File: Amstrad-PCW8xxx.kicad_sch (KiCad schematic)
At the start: 103 parts, among them IC101 GateArray, IC102 Z80A, IC103 74HCU04, IC120 TC74HC14, IC201 SED9420AC, IC202 74HC00, IC204 74HC04, IC205 74HC04, J101 Printer Power, X101 32MHz, X201 18MHz, X701 11MHz

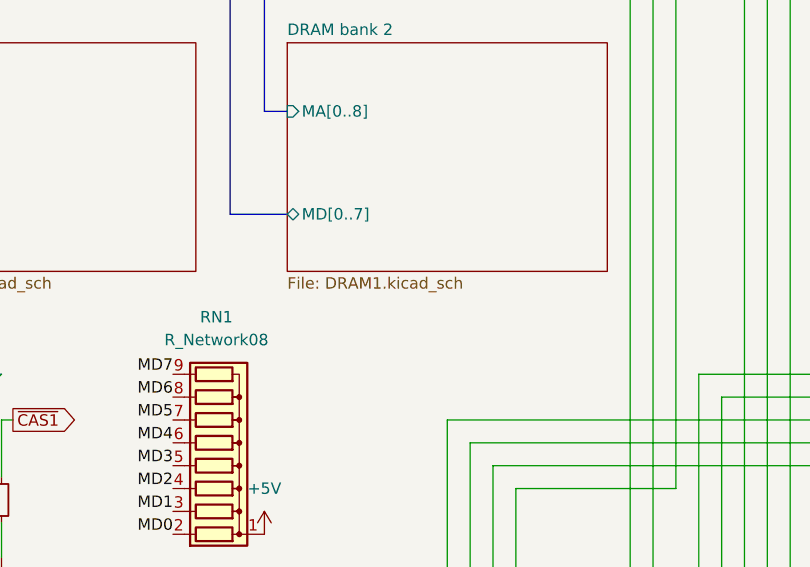
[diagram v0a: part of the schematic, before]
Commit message: fix shared schematic across dram pages
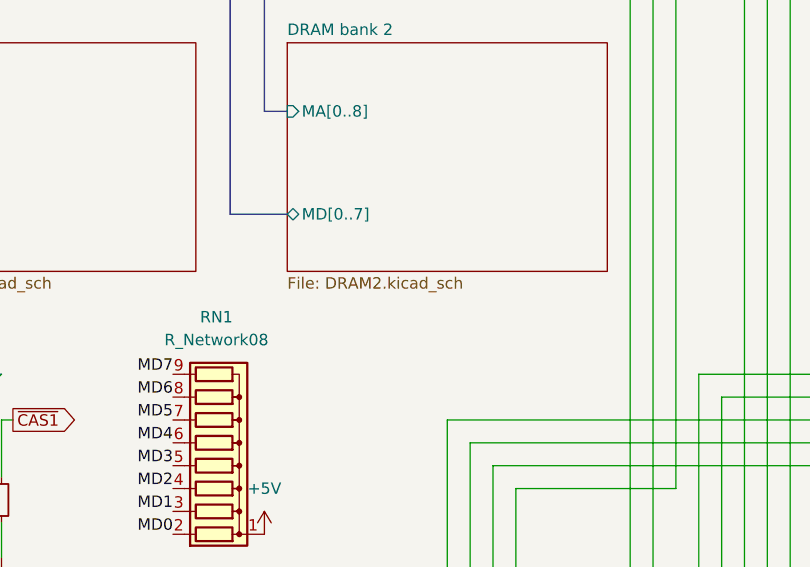
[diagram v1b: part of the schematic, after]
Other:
- sheet DRAM bank 2: file DRAM1.kicad_sch -> DRAM2.kicad_sch
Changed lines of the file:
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@@
 			)
 		)
-		(property "Sheetfile" "DRAM1.kicad_sch"
+		(property "Sheetfile" "DRAM2.kicad_sch"
 			(at 242.57 146.6346 0)
 			(show_name no)

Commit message: fix incorrect gate array pin numbering
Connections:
- net +5V: now also IC102.11 (V_{CC})
- net MA5: now also R115.1
- net ~{CAS1}: no longer R104.1
- net at R103.2: now also IC101.8 (~{MWE}); no longer IC101.19 (~{MWE})
- net at R105.2: now also IC101.16 (~{CAS1}); no longer IC101.8 (~{CAS1})
- net at IC203.16 (TC): now also IC101.18 (TC); no longer IC101.16 (TC)
- net at IC203.2 (~{RD}): now also IC101.19 (~{DIORD}); no longer IC101.18 (~{DIORD})
- net at R115.2: now also IC101.36 (MA5)
- new net ~{CAS2}: R104.1
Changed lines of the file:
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@@
 	)
 	(no_connect
-		(at 90.17 177.8)
+		(at 90.17 172.72)
 	)
 	(no_connect
@@
 	)
 	(no_connect
-		(at 92.71 177.8)
+		(at 92.71 172.72)
 	)
 	(no_connect
@@
 	(wire
 		(pts
+			(xy 158.75 172.72) (xy 158.75 177.8)
+		)
+		(stroke
+			(width 0)
+			(type default)
+		)
+	)
+	(wire
+		(pts
 			(xy 49.53 180.34) (xy 74.93 180.34)
 		)
@@
 	(wire
 		(pts
-			(xy 158.75 160.02) (xy 158.75 163.83)
+			(xy 158.75 160.02) (xy 158.75 167.64)
 		)
 		(stroke
@@
 		)
 	)
-	(global_label "~{CAS1}"
+	(global_label "~{CAS2}"
 		(shape output)
 		(at 212.09 162.56 0)
@@
 	(symbol
 		(lib_id "power:+5V")
-		(at 87.63 177.8 0)
+		(at 87.63 172.72 0)
 		(unit 1)
 		(body_style 1)
@@
 		(fields_autoplaced yes)
 		(property "Reference" "#PWR010"
-			(at 87.63 181.61 0)
+			(at 87.63 176.53 0)
 			(hide yes)
 			(show_name no)
@@
 		)
 		(property "Value" "+5V"
-			(at 87.63 172.72 0)
+			(at 87.63 167.64 0)
 			(show_name no)
 			(do_not_autoplace no)
@@
 		)
 		(property "Footprint" ""
-			(at 87.63 177.8 0)
+			(at 87.63 172.72 0)
 			(hide yes)
 			(show_name no)
@@
 		)
 		(property "Datasheet" ""
-			(at 87.63 177.8 0)
+			(at 87.63 172.72 0)
 			(hide yes)
 			(show_name no)
@@
 		)
 		(property "Description" "Power symbol creates a global label with name \"+5V\""
-			(at 87.63 177.8 0)
+			(at 87.63 172.72 0)
 			(hide yes)
 			(show_name no)
@@
 	(symbol
 		(lib_id "Device:R_Small")
-		(at 158.6374 170.135 0)
+		(at 158.75 170.18 0)
 		(unit 1)
 		(body_style 1)
@@
 		(dnp no)
 		(property "Reference" "R115"
-			(at 157.6214 176.4849 90)
+			(at 157.734 176.5299 90)
 			(show_name no)
 			(do_not_autoplace no)
@@
 		)
 		(property "Value" "33R"
-			(at 157.6214 167.8489 90)
+			(at 157.734 167.8939 90)
 			(show_name no)
 			(do_not_autoplace no)
@@
 		)
 		(property "Footprint" ""
-			(at 158.6374 170.135 0)
+			(at 158.75 170.18 0)
 			(hide yes)
 			(show_name no)
@@
 		)
 		(property "Datasheet" ""
-			(at 158.6374 170.135 0)
+			(at 158.75 170.18 0)
 			(hide yes)
 			(show_name no)
@@
 		)
 		(property "Description" "Resistor, small symbol"
-			(at 158.6374 170.135 0)
+			(at 158.75 170.18 0)
 			(hide yes)
 			(show_name no)

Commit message: outline pcb
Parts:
- removed C201: 100nF, symbol Device:C_Small
- removed CP103: Keyboard Connector, symbol Connector:DIN-4
- added CP103: Keyboard Connection, Connector_Molex:Molex_KK-254_AE-6410-04A_1x04_P2.54mm_Vertical, symbol Connector_Generic:Conn_01x04
- C101, C102, C103, C104, C105, C106, C107, C108, C109, C110, C111, C112, C113, C114, C115, C116, C117, C118, C119, C120, C126, C127, C128, C201, C202, C203, C204, C205, C206, C207, C208, C209, C210, C701, C702, C703: footprint (none) -> Capacitor_THT:C_Disc_D10.0mm_W2.5mm_P5.00mm
- C121: footprint (none) -> Capacitor_THT:CP_Radial_D10.0mm_P5.00mm; now left out of the parts list
- C122, C123, C124: footprint (none) -> Capacitor_THT:CP_Radial_D10.0mm_P5.00mm
- CD201, CD202, CP101: footprint (none) -> Connector_Molex:Molex_KK-254_AE-6410-04A_1x04_P2.54mm_Vertical
- CD203: footprint (none) -> Connector_IDC:IDC-Header_2x13_P2.54mm_Horizontal
- CP706: footprint Connector_PinSocket_2.54mm:PinSocket_2x17_P2.54mm_Horizontal -> Connector_IDC:IDC-Header_2x17_P2.54mm_Horizontal
- IC101: footprint (none) -> Package_QFP:Hitachi_FP80B_PQFP-80_14x20mm_P0.8mm
- IC103, IC120, IC202, IC204, IC205: footprint (none) -> Package_DIP:DIP-14_W7.62mm
- IC201: footprint (none) -> Package_DIP:DIP-24_18.0mmx34.29mm_W15.24mm
- IC203: value (none) -> D765AC-2; footprint (none) -> Package_DIP:DIP-40_W15.24mm
- IC701: value (none) -> 40026; footprint (none) -> Package_DIP:DIP-40_W15.24mm
- NR103: renamed from RN1; value R_Network08 -> 10K
- R101, R102, R103, R104, R105, R106, R107, R108, R109, R110, R111, R112, R113, R114, R115, R116, R117, R118, R119, R120, R122, R123, R124, R201, R202, R203, R204, R206, R701, R725: footprint (none) -> Resistor_THT:R_Axial_DIN0207_L6.3mm_D2.5mm_P10.16mm_Horizontal
- X101: footprint (none) -> Crystal:Crystal_HC49-U_Horizontal_1EP_style2
- X201, X701: footprint (none) -> Crystal:Crystal_HC52-8mm_Vertical
- renumbered NR202 to NR102
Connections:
- net +5V: now also CP103.2 (Pin_2)
- net GND: now also CP103.1 (Pin_1)
- net K3: now also CP103.3 (Pin_3)
- net K4: now also CP103.4 (Pin_4)
- net at IC202.10, IC203.39 (~{RW}/SEEK), NR201.8 (R7): now also IC202.12
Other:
- moved on the sheet: IC204B, IC204E, IC205A, IC205B

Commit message: progress PCB layout
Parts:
- C101, C102, C103, C104, C105, C106, C107, C108, C109, C110, C111, C112, C113, C114, C115, C116, C117, C118, C119, C120, C126, C127, C128, C201, C202, C203, C204, C205, C206, C207, C208, C209, C210, C701, C702, C703: footprint Capacitor_THT:C_Disc_D10.0mm_W2.5mm_P5.00mm -> Library:C_Disc_D9.0mm_W2.5mm_P5.00mm
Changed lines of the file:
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@@
 			)
 		)
-		(property "Footprint" "Capacitor_THT:C_Disc_D10.0mm_W2.5mm_P5.00mm"
+		(property "Footprint" "Library:C_Disc_D9.0mm_W2.5mm_P5.00mm"
 			(at 170.18 323.85 0)
 			(hide yes)
@@
 			)
 		)
-		(property "Footprint" "Capacitor_THT:C_Disc_D10.0mm_W2.5mm_P5.00mm"
+		(property "Footprint" "Library:C_Disc_D9.0mm_W2.5mm_P5.00mm"
 			(at 223.52 323.85 0)
 			(hide yes)
@@
 			)
 		)
-		(property "Footprint" "Capacitor_THT:C_Disc_D10.0mm_W2.5mm_P5.00mm"
+		(property "Footprint" "Library:C_Disc_D9.0mm_W2.5mm_P5.00mm"
 			(at 193.04 323.85 0)
 			(hide yes)
@@
 			)
 		)
-		(property "Footprint" "Capacitor_THT:C_Disc_D10.0mm_W2.5mm_P5.00mm"
+		(property "Footprint" "Library:C_Disc_D9.0mm_W2.5mm_P5.00mm"
 			(at 215.9 323.85 0)
 			(hide yes)
@@
 			)
 		)
-		(property "Footprint" "Capacitor_THT:C_Disc_D10.0mm_W2.5mm_P5.00mm"
+		(property "Footprint" "Library:C_Disc_D9.0mm_W2.5mm_P5.00mm"
 			(at 447.04 294.64 0)
 			(hide yes)
@@
 			)
 		)
-		(property "Footprint" "Capacitor_THT:C_Disc_D10.0mm_W2.5mm_P5.00mm"
+		(property "Footprint" "Library:C_Disc_D9.0mm_W2.5mm_P5.00mm"
 			(at 471.17 226.06 0)
 			(hide yes)
@@
 			)
 		)
-		(property "Footprint" "Capacitor_THT:C_Disc_D10.0mm_W2.5mm_P5.00mm"
+		(property "Footprint" "Library:C_Disc_D9.0mm_W2.5mm_P5.00mm"
 			(at 88.9 120.65 0)
 			(hide yes)
@@
 			)
 		)
-		(property "Footprint" "Capacitor_THT:C_Disc_D10.0mm_W2.5mm_P5.00mm"
+		(property "Footprint" "Library:C_Disc_D9.0mm_W2.5mm_P5.00mm"
 			(at 162.56 334.01 0)
 			(hide yes)
@@
 			)
 		)
-		(property "Footprint" "Capacitor_THT:C_Disc_D10.0mm_W2.5mm_P5.00mm"
+		(property "Footprint" "Library:C_Disc_D9.0mm_W2.5mm_P5.00mm"
 			(at 473.71 250.19 0)
 			(hide yes)
@@
 			)
 		)
-		(property "Footprint" "Capacitor_THT:C_Disc_D10.0mm_W2.5mm_P5.00mm"
+		(property "Footprint" "Library:C_Disc_D9.0mm_W2.5mm_P5.00mm"
 			(at 200.66 323.85 0)
 			(hide yes)
@@
 			)
 		)
-		(property "Footprint" "Capacitor_THT:C_Disc_D10.0mm_W2.5mm_P5.00mm"
+		(property "Footprint" "Library:C_Disc_D9.0mm_W2.5mm_P5.00mm"
 			(at 208.28 323.85 0)
 			(hide yes)
@@
 			)
 		)
-		(property "Footprint" "Capacitor_THT:C_Disc_D10.0mm_W2.5mm_P5.00mm"
+		(property "Footprint" "Library:C_Disc_D9.0mm_W2.5mm_P5.00mm"
 			(at 238.76 323.85 0)
 			(hide yes)
@@
 			)
 		)
-		(property "Footprint" "Capacitor_THT:C_Disc_D10.0mm_W2.5mm_P5.00mm"
+		(property "Footprint" "Library:C_Disc_D9.0mm_W2.5mm_P5.00mm"
 			(at 299.72 294.64 0)
 			(hide yes)
@@
 			)
 		)
-		(property "Footprint" "Capacitor_THT:C_Disc_D10.0mm_W2.5mm_P5.00mm"
+		(property "Footprint" "Library:C_Disc_D9.0mm_W2.5mm_P5.00mm"
 			(at 254 323.85 0)
 			(hide yes)
@@
 			)
 		)
-		(property "Footprint" "Capacitor_THT:C_Disc_D10.0mm_W2.5mm_P5.00mm"
+		(property "Footprint" "Library:C_Disc_D9.0mm_W2.5mm_P5.00mm"
 			(at 469.9 260.35 0)
 			(hide yes)
@@
 			)
 		)
-		(property "Footprint" "Capacitor_THT:C_Disc_D10.0mm_W2.5mm_P5.00mm"
+		(property "Footprint" "Library:C_Disc_D9.0mm_W2.5mm_P5.00mm"
 			(at 276.86 323.85 0)
 			(hide yes)
@@
 			)
 		)
-		(property "Footprint" "Capacitor_THT:C_Disc_D10.0mm_W2.5mm_P5.00mm"
+		(property "Footprint" "Library:C_Disc_D9.0mm_W2.5mm_P5.00mm"
 			(at 185.42 323.85 0)
 			(hide yes)
@@
 			)
 		)
-		(property "Footprint" "Capacitor_THT:C_Disc_D10.0mm_W2.5mm_P5.00mm"
+		(property "Footprint" "Library:C_Disc_D9.0mm_W2.5mm_P5.00mm"
 			(at 246.38 323.85 0)
 			(hide yes)
@@
 			)
 		)
-		(property "Footprint" "Capacitor_THT:C_Disc_D10.0mm_W2.5mm_P5.00mm"
+		(property "Footprint" "Library:C_Disc_D9.0mm_W2.5mm_P5.00mm"
 			(at 68.58 130.81 0)
 			(hide yes)
@@
 			)
 		)
-		(property "Footprint" "Capacitor_THT:C_Disc_D10.0mm_W2.5mm_P5.00mm"
+		(property "Footprint" "Library:C_Disc_D9.0mm_W2.5mm_P5.00mm"
 			(at 231.14 323.85 0)
 			(hide yes)
@@
 			)
 		)
-		(property "Footprint" "Capacitor_THT:C_Disc_D10.0mm_W2.5mm_P5.00mm"
+		(property "Footprint" "Library:C_Disc_D9.0mm_W2.5mm_P5.00mm"
 			(at 147.32 323.85 0)
 			(hide yes)
@@
 			)
 		)
-		(property "Footprint" "Capacitor_THT:C_Disc_D10.0mm_W2.5mm_P5.00mm"
+		(property "Footprint" "Library:C_Disc_D9.0mm_W2.5mm_P5.00mm"
 			(at 177.8 323.85 0)
 			(hide yes)
@@
 			)
 		)
-		(property "Footprint" "Capacitor_THT:C_Disc_D10.0mm_W2.5mm_P5.00mm"
+		(property "Footprint" "Library:C_Disc_D9.0mm_W2.5mm_P5.00mm"
 			(at 471.17 238.76 0)
 			(hide yes)
@@
 			)
 		)
-		(property "Footprint" "Capacitor_THT:C_Disc_D10.0mm_W2.5mm_P5.00mm"
+		(property "Footprint" "Library:C_Disc_D9.0mm_W2.5mm_P5.00mm"
 			(at 139.7 323.85 0)
 			(hide yes)
@@
 			)
 		)
-		(property "Footprint" "Capacitor_THT:C_Disc_D10.0mm_W2.5mm_P5.00mm"
+		(property "Footprint" "Library:C_Disc_D9.0mm_W2.5mm_P5.00mm"
 			(at 269.24 323.85 0)
 			(hide yes)
@@
 			)
 		)
-		(property "Footprint" "Capacitor_THT:C_Disc_D10.0mm_W2.5mm_P5.00mm"
+		(property "Footprint" "Library:C_Disc_D9.0mm_W2.5mm_P5.00mm"
 			(at 162.56 323.85 0)
 			(hide yes)
@@
 			)
 		)
-		(property "Footprint" "Capacitor_THT:C_Disc_D10.0mm_W2.5mm_P5.00mm"
+		(property "Footprint" "Library:C_Disc_D9.0mm_W2.5mm_P5.00mm"
 			(at 132.08 323.85 0)
 			(hide yes)
@@
 			)
 		)
-		(property "Footprint" "Capacitor_THT:C_Disc_D10.0mm_W2.5mm_P5.00mm"
+		(property "Footprint" "Library:C_Disc_D9.0mm_W2.5mm_P5.00mm"
 			(at 147.32 334.01 0)
 			(hide yes)
@@
 			)
 		)
-		(property "Footprint" "Capacitor_THT:C_Disc_D10.0mm_W2.5mm_P5.00mm"
+		(property "Footprint" "Library:C_Disc_D9.0mm_W2.5mm_P5.00mm"
 			(at 154.94 334.01 0)
 			(hide yes)
@@
 			)
 		)
-		(property "Footprint" "Capacitor_THT:C_Disc_D10.0mm_W2.5mm_P5.00mm"
+		(property "Footprint" "Library:C_Disc_D9.0mm_W2.5mm_P5.00mm"
 			(at 487.68 254 0)
 			(hide yes)
@@
 			)
 		)
-		(property "Footprint" "Capacitor_THT:C_Disc_D10.0mm_W2.5mm_P5.00mm"
+		(property "Footprint" "Library:C_Disc_D9.0mm_W2.5mm_P5.00mm"
 			(at 307.34 298.45 0)
 			(hide yes)
@@
 			)
 		)
-		(property "Footprint" "Capacitor_THT:C_Disc_D10.0mm_W2.5mm_P5.00mm"
+		(property "Footprint" "Library:C_Disc_D9.0mm_W2.5mm_P5.00mm"
 			(at 154.94 323.85 0)
 			(hide yes)
@@
 			)
 		)
-		(property "Footprint" "Capacitor_THT:C_Disc_D10.0mm_W2.5mm_P5.00mm"
+		(property "Footprint" "Library:C_Disc_D9.0mm_W2.5mm_P5.00mm"
 			(at 261.62 323.85 0)
 			(hide yes)
@@
 			)
 		)
-		(property "Footprint" "Capacitor_THT:C_Disc_D10.0mm_W2.5mm_P5.00mm"
+		(property "Footprint" "Library:C_Disc_D9.0mm_W2.5mm_P5.00mm"
 			(at 139.7 334.01 0)
 			(hide yes)
@@
 			)
 		)
-		(property "Footprint" "Capacitor_THT:C_Disc_D10.0mm_W2.5mm_P5.00mm"
+		(property "Footprint" "Library:C_Disc_D9.0mm_W2.5mm_P5.00mm"
 			(at 172.72 334.01 0)
 			(hide yes)
@@
 			)
 		)
-		(property "Footprint" "Capacitor_THT:C_Disc_D10.0mm_W2.5mm_P5.00mm"
+		(property "Footprint" "Library:C_Disc_D9.0mm_W2.5mm_P5.00mm"
 			(at 88.9 130.81 0)
 			(hide yes)

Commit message: layout pcb components
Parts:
- added D102, D103: (no value), Diode_THT:D_DO-35_SOD27_P10.16mm_Horizontal, symbol Device:D_Schottky_Small_Filled
- added R121: 2K2, Library:R_Axial_DIN0207_L6.3mm_D2.5mm_P10.16mm_Horizontal, symbol Device:R_Small
- C121: now in the parts list
- C123: footprint Capacitor_THT:CP_Radial_D10.0mm_P5.00mm -> Library:C_Disc_D9.0mm_W2.5mm_P5.00mm
- D101: footprint (none) -> Library:D_DO-35_SOD27_P10.16mm_Horizontal
- R101, R102, R103, R104, R105, R106, R107, R108, R109, R110, R111, R112, R113, R114, R115, R116, R117, R118, R119, R120, R122, R123, R124, R201, R202, R203, R204, R206, R701, R725: footprint Resistor_THT:R_Axial_DIN0207_L6.3mm_D2.5mm_P10.16mm_Horizontal -> Library:R_Axial_DIN0207_L6.3mm_D2.5mm_P10.16mm_Horizontal
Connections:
- net +5V: now also R121.1
- net E35: now also R121.2
- net GND: now also D102.2 (A), D103.2 (A)
- net K3: now also D103.1 (K)
- net K4: now also D102.1 (K)

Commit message: finish up PCB layout
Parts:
- removed LK2: (no value), symbol library:link
- removed NR107: 10K, Resistor_THT:R_Array_SIP5, symbol Device:R_Network04
- removed NR202: 680R, Resistor_THT:R_Array_SIP6, symbol Device:R_Network05
- added unit 3 of NR102
- added unit 1 of NR102
- added unit 4 of NR102
- added unit 2 of NR102
- added NR202: 680R, Resistor_THT:R_Array_SIP8, symbol Device:R_Network07
- C121, C122, C124: footprint Capacitor_THT:CP_Radial_D10.0mm_P5.00mm -> Library:CP_Radial_P5.00mm
- CD203: footprint Connector_IDC:IDC-Header_2x13_P2.54mm_Horizontal -> Connector_IDC:IDC-Header_2x13_P2.54mm_Vertical
- CP100: footprint (none) -> Library:Power Connection
- IC101: footprint Package_QFP:Hitachi_FP80B_PQFP-80_14x20mm_P0.8mm -> Library:Amstrad_PQFP-80_14x20mm_P0.8mm
- IC201: footprint Package_DIP:DIP-24_18.0mmx34.29mm_W15.24mm -> Package_DIP:DIP-28_W15.24mm
- J101: footprint (none) -> Connector_BarrelJack:BarrelJack_Horizontal
- L101: footprint (none) -> Inductor_THT:L_Axial_L6.6mm_D2.7mm_P10.16mm_Horizontal_Vishay_IM-2
- LK1: footprint (none) -> Library:Link_2; symbol library:link -> Library:link_2T
- LS1: footprint (none) -> Library:Speaker
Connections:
- net +12V: now also CP100.2 (Pin_2); no longer CP100.4 (Pin_4)
- net +5V: now also LK1.A, LK1.C, NR102.1 (R1), NR102.1 (R1), NR102.1 (R1), NR102.1 (R1), NR202.1 (common); no longer LK1.2 (B)
- net E34: now also NR102.4 (R3.2)
- net E40: now also NR102.2 (R1.2)
- net E41: now also NR102.5 (R4.2)
- net E42: now also NR102.3 (R2.2)
- net F18: now also NR202.2 (R1)
- net F2: now also NR202.4 (R3)
- net F20: now also NR202.3 (R2)
- net F22: now also NR202.6 (R5)
- net F26: now also NR202.5 (R4)
- net GND: now also CP100.4 (Pin_4), CP100.5 (Pin_5), LK1.B, LK1.D; no longer CP100.1 (Pin_1), CP100.2 (Pin_2), LK1.1 (A)
- net at R108.1: now also LK1.2
- net at C123.1, J101.2 (Pin_2): now also CP100.1 (Pin_1); no longer CP100.5 (Pin_5)
- net at R107.1: now also LK1.1; no longer LK1.3 (C)
- no-connect marks 17 -> 19
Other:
- note removed: "A"
- note removed: "B"
- note removed: "C"
- note removed: "D"
- moved on the sheet: CP100, IC205E, R108
